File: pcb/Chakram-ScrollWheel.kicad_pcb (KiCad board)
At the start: 2 copper layers, 39.7 x 22.5 mm, 26 parts, among them J1 FPC Connector

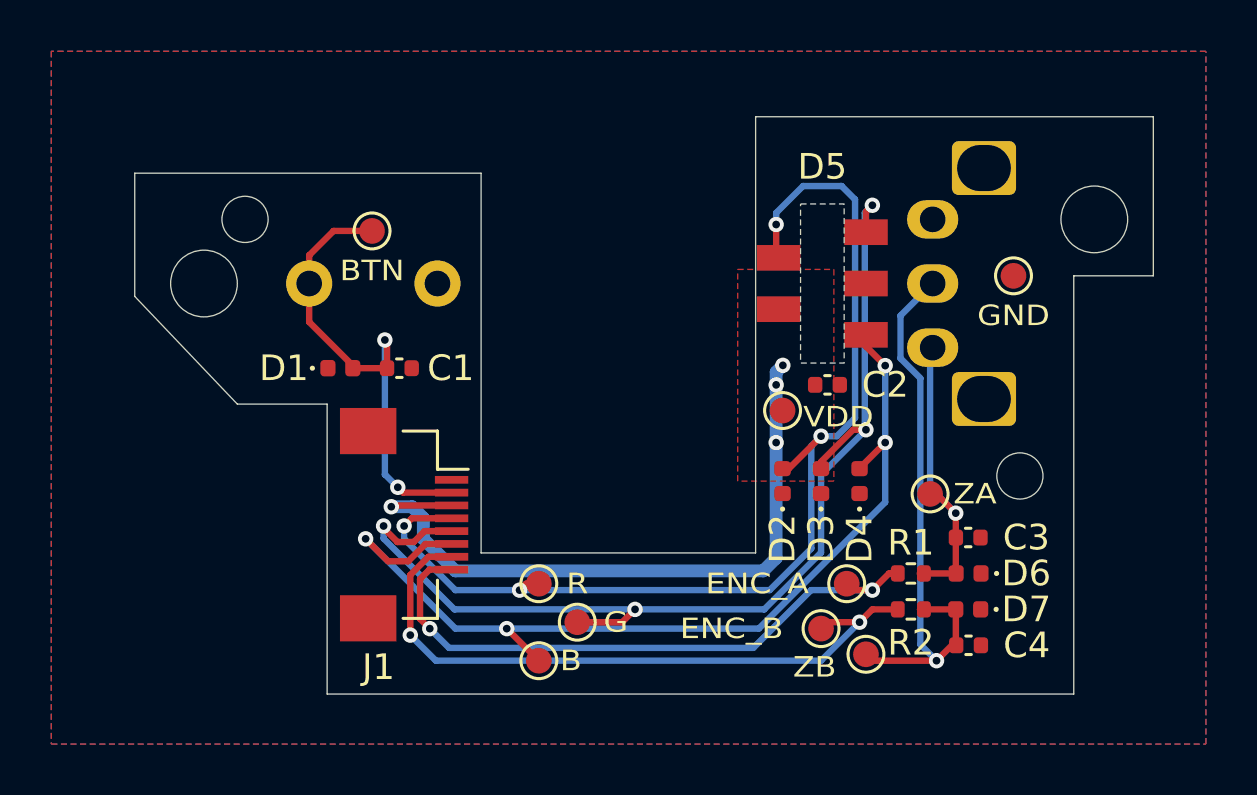
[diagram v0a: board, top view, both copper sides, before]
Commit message: Added button part name to silkscreen
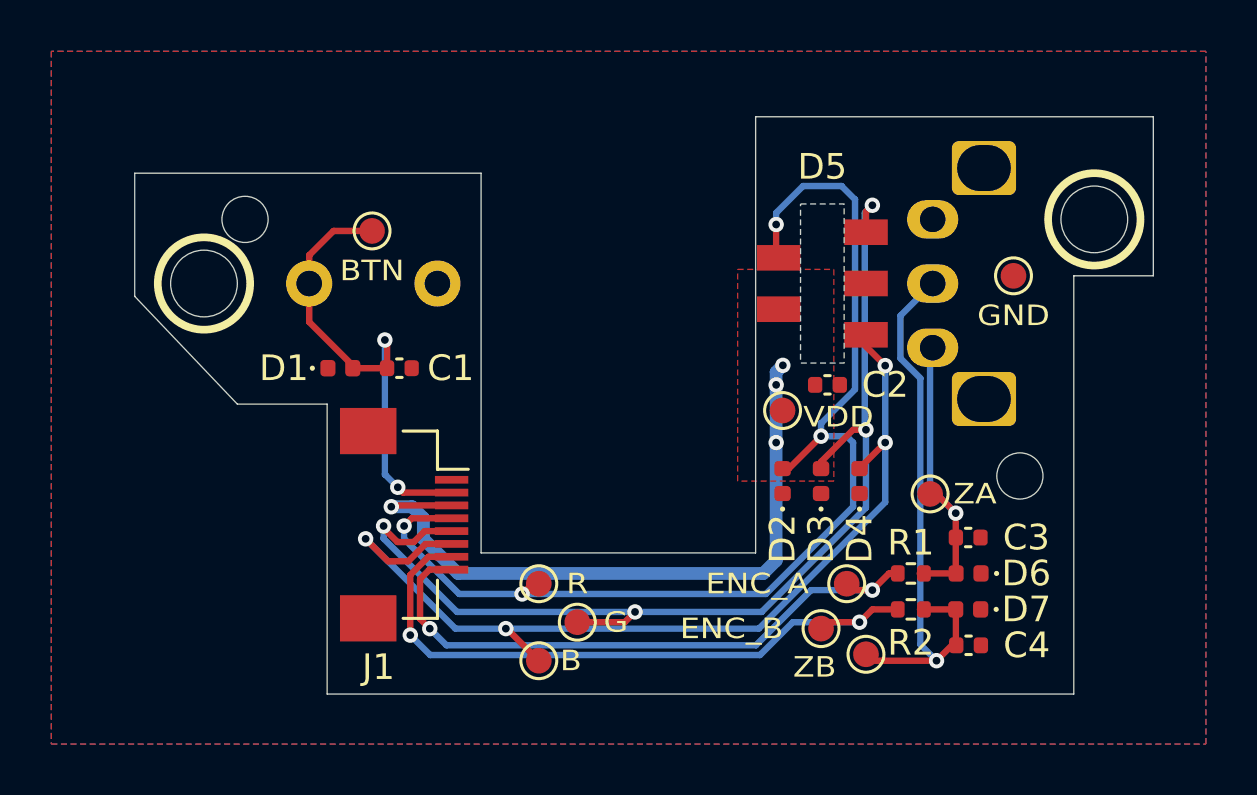
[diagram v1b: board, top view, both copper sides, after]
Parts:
- added REF**: Logo_Moucha_3x3mm_SilkScreen, Moucha_Graphics:Logo_Moucha_3x3mm_SilkScreen, B.Cu at (88.0, 71.8)
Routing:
- net /LED_R: track 42.9 -> 44.3 mm
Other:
- board text added: "EVQP0"
- board text added: "SM9381 WHEEL PCB"
- board text added: "v${REVISION} ${ISSUE_DATE}"

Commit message: Added more silkscreen elements, minor cleanups
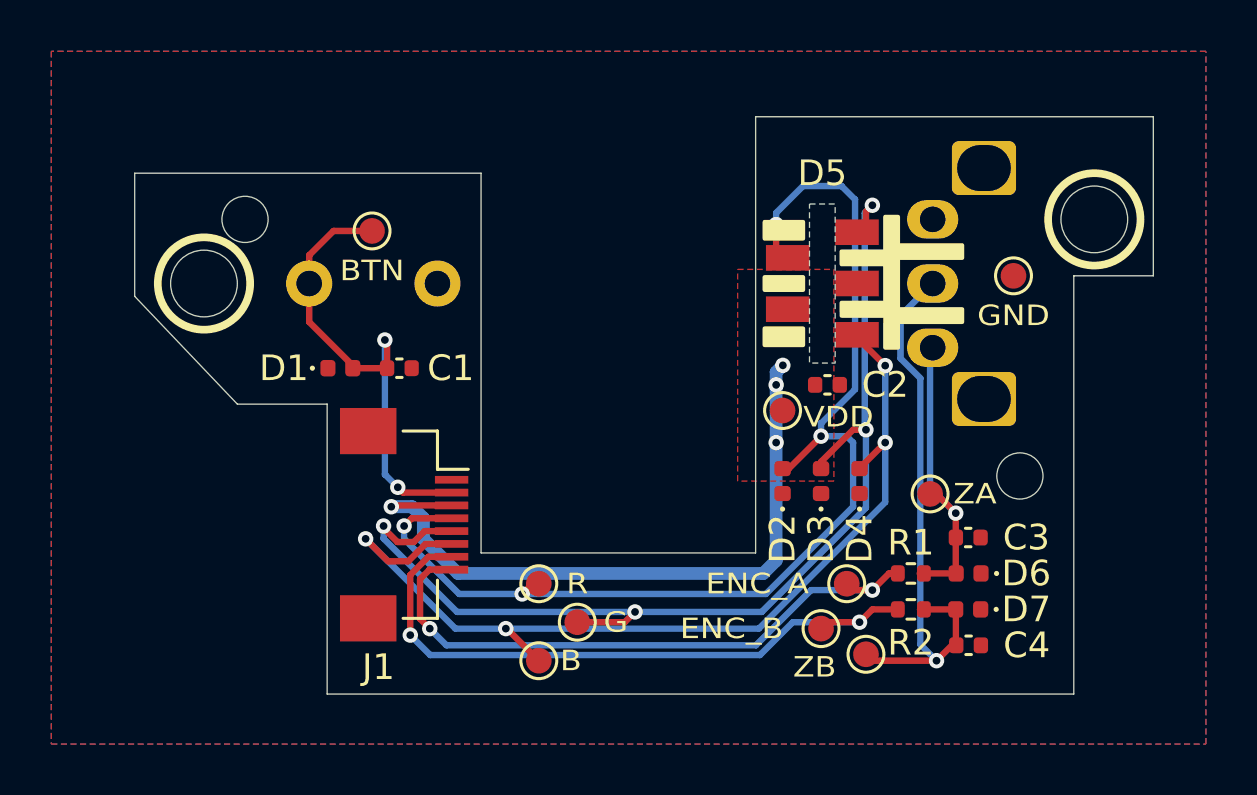
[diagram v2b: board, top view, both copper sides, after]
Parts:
- moved REF** 0.57 mm to (87.5, 72.0)
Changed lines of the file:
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@@
 	)
 	(footprint "Moucha_Modules:LED_Chakram"
-		(locked yes)
 		(layer "F.Cu")
 		(at 81.8 59.3)
 		(property "Reference" "D5"
-			(at 0 -4.55 0)
+			(at 0 -4.3 0)
 			(unlocked yes)
 			(layer "F.SilkS")
@@
 			(effects
 				(font
-					(size 0.8 0.9)
+					(size 1 1)
 					(thickness 0.15)
 				)
@@
 		(sheetfile "Chakram-ScrollWheel.kicad_sch")
 		(fp_rect
-			(start -0.85 -3.1)
-			(end 0.85 3.1)
+			(start -0.5 -3.1)
+			(end 0.5 3.1)
 			(stroke
 				(width 0.05)
@@
 		)
 		(fp_rect
-			(start -1 -7.5)
-			(end 1 7.5)
+			(start -0.7 -6.5)
+			(end 0.7 6.5)
 			(stroke
 				(width 0.05)
@@
 		)
 		(fp_rect
-			(start -2.7 -3.2)
-			(end 2.7 3.2)
+			(start -2.4 -3.2)
+			(end 2.4 3.2)
 			(stroke
 				(width 0.05)
@@
 		)
 		(fp_text user "${REFERENCE}"
-			(at 0 4.2 0)
+			(at 0 -4.3 0)
 			(unlocked yes)
 			(layer "F.Fab")
@@
 		)
 		(pad "1" connect rect
-			(at 1.7 -2)
+			(at 1.35 -2)
 			(size 1.7 1)
 			(layers "F.Cu" "F.Mask")
@@
 		)
 		(pad "2" connect rect
-			(at 1.7 0)
+			(at 1.35 0)
 			(size 1.7 1)
 			(layers "F.Cu" "F.Mask")
@@
 		)
 		(pad "3" connect rect
-			(at 1.7 2)
+			(at 1.35 2)
 			(size 1.7 1)
 			(layers "F.Cu" "F.Mask")
@@
 		)
 		(pad "4" connect rect
-			(at -1.7 -1)
+			(at -1.35 -1)
 			(size 1.7 1)
 			(layers "F.Cu" "F.Mask")
@@
 		)
 		(pad "5" connect rect
-			(at -1.7 1)
+			(at -1.35 1)
 			(size 1.7 1)
 			(layers "F.Cu" "F.Mask")
@@
 	(footprint "Moucha_Graphics:Logo_Moucha_3x3mm_SilkScreen"
 		(layer "B.Cu")
-		(at 88 71.75 -135)
+		(at 87.485 72 -135)
 		(descr "Petr Moucha Logo")
 		(tags "Logo Moucha")
@@
 		(layer "F.SilkS")
 	)
+	(gr_rect
+		(start 79.55 59.05)
+		(end 81.05 59.55)
+		(stroke
+			(width 0.16)
+			(type solid)
+		)
+		(fill solid)
+		(layer "F.SilkS")
+	)
+	(gr_rect
+		(start 79.55 56.9)
+		(end 81.05 57.55)
+		(stroke
+			(width 0.16)
+			(type solid)
+		)
+		(fill solid)
+		(layer "F.SilkS")
+	)
+	(gr_poly
+		(pts
+			(xy 84.25 56.7) (xy 84.75 56.7) (xy 84.75 57.809106) (xy 87.25 57.809106) (xy 87.25 58.3) (xy 84.75 58.3)
+			(xy 84.75 60.3) (xy 87.25 60.3) (xy 87.25 60.8) (xy 84.75 60.8) (xy 84.75 61.8) (xy 84.25 61.8) (xy 84.252472 60.557414)
+			(xy 82.552472 60.557414) (xy 82.55 60.05) (xy 84.25 60.05) (xy 84.25 58.55) (xy 82.55 58.55) (xy 82.55 58.05)
+			(xy 84.25 58.05)
+		)
+		(stroke
+			(width 0.16)
+			(type solid)
+		)
+		(fill solid)
+		(layer "F.SilkS")
+	)
 	(gr_circle
 		(center 57.7 59.3)
@@
 		(layer "F.SilkS")
 	)
+	(gr_rect
+		(start 79.55 61.05)
+		(end 81.05 61.7)
+		(stroke
+			(width 0.16)
+			(type solid)
+		)
+		(fill solid)
+		(layer "F.SilkS")
+	)
 	(gr_line
 		(start 91.6 75.3)
@@
 	)
 	(segment
-		(start 86 67.5)
-		(end 86.25 67.5)
-		(width 0.25)
-		(layer "F.Cu")
-		(net 2)
-	)
-	(segment
 		(start 87 68.25)
 		(end 87 70.585)
@@
 	)
 	(segment
-		(start 87 70.585)
-		(end 87.015 70.6)
-		(width 0.25)
-		(layer "F.Cu")
-		(net 2)
-	)
-	(segment
 		(start 87.015 70.6)
 		(end 85.595 70.6)
@@
 	)
 	(segment
-		(start 86 61.9)
-		(end 86.1 61.8)
-		(width 0.25)
-		(layer "B.Cu")
-		(net 2)
-	)
-	(segment
 		(start 86 67.25)
 		(end 86 61.9)
@@
 	)
 	(segment
-		(start 87.005 72.005)
-		(end 87 72)
-		(width 0.25)
-		(layer "F.Cu")
-		(net 3)
-	)
-	(segment
-		(start 86.884337 73.365663)
-		(end 87.015568 73.365663)
-		(width 0.25)
-		(layer "F.Cu")
-		(net 3)
-	)
-	(segment
 		(start 86.25 74)
 		(end 83.5 74)
@@
 		(net 3)
 	)
-	(segment
-		(start 87.015568 73.365663)
-		(end 87.005 73.355095)
-		(width 0.25)
-		(layer "F.Cu")
-		(net 3)
-	)
 	(via
 		(at 86.25 74)
@@
 		(net 4)
 	)
-	(segment
-		(start 63.5 62.5)
-		(end 63.5 62.6)
-		(width 0.25)
-		(layer "F.Cu")
-		(net 4)
-	)
 	(via
 		(at 64.75 61.5)
@@
 	)
 	(segment
-		(start 80 58.2)
-		(end 80.1 58.3)
-		(width 0.25)
-		(layer "F.Cu")
-		(net 6)
-	)
-	(segment
 		(start 70.1 71.4)
 		(end 70.5 71)
@@
 		(net 6)
 	)
-	(segment
-		(start 70.5 71)
-		(end 70.75 71)
-		(width 0.25)
-		(layer "F.Cu")
-		(net 6)
-	)
 	(via
 		(at 81.75 65.25)
@@
 	)
 	(segment
-		(start 83.25 66.5)
-		(end 83.25 66.515)
-		(width 0.25)
-		(layer "F.Cu")
-		(net 7)
-	)
-	(segment
 		(start 84.25 65.5)
 		(end 83.25 66.5)
@@
 		(net 9)
 	)
-	(segment
-		(start 82 72.5)
-		(end 81.75 72.75)
-		(width 0.25)
-		(layer "F.Cu")
-		(net 9)
-	)
 	(via
 		(at 83.25 72.5)
@@
 	)
 	(segment
-		(start 83 71.25)
-		(end 82.75 71)
-		(width 0.25)
-		(layer "F.Cu")
-		(net 10)
-	)
-	(segment

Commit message: Added ground stitching
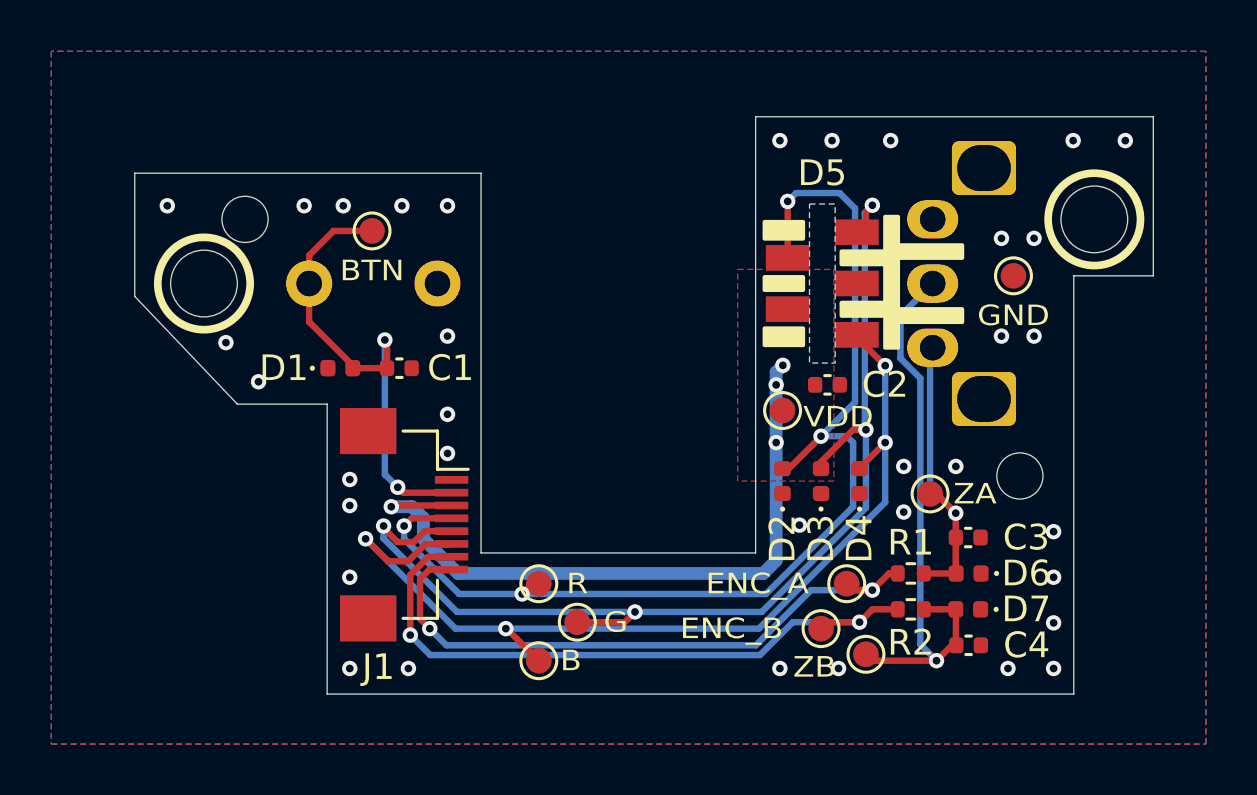
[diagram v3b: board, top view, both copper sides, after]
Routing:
- net /LED_R: track 43.9 -> 43.4 mm
- net GND: vias 0 -> 35
